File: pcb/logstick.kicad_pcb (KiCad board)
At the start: 2 copper layers, 12 parts, among them IC1 ATTINY85-P, K1 USB, K2 DHT44, K3 SWITCH

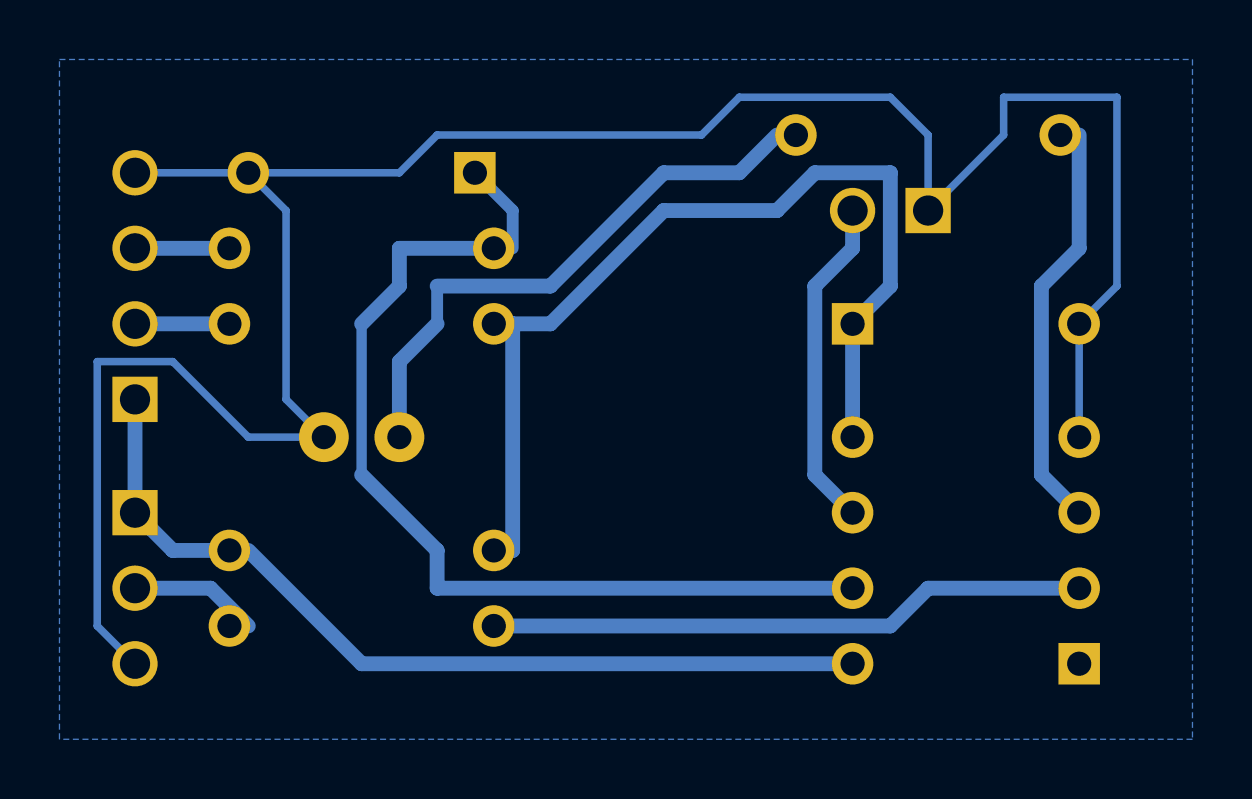
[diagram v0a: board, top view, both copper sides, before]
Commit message: correction R68
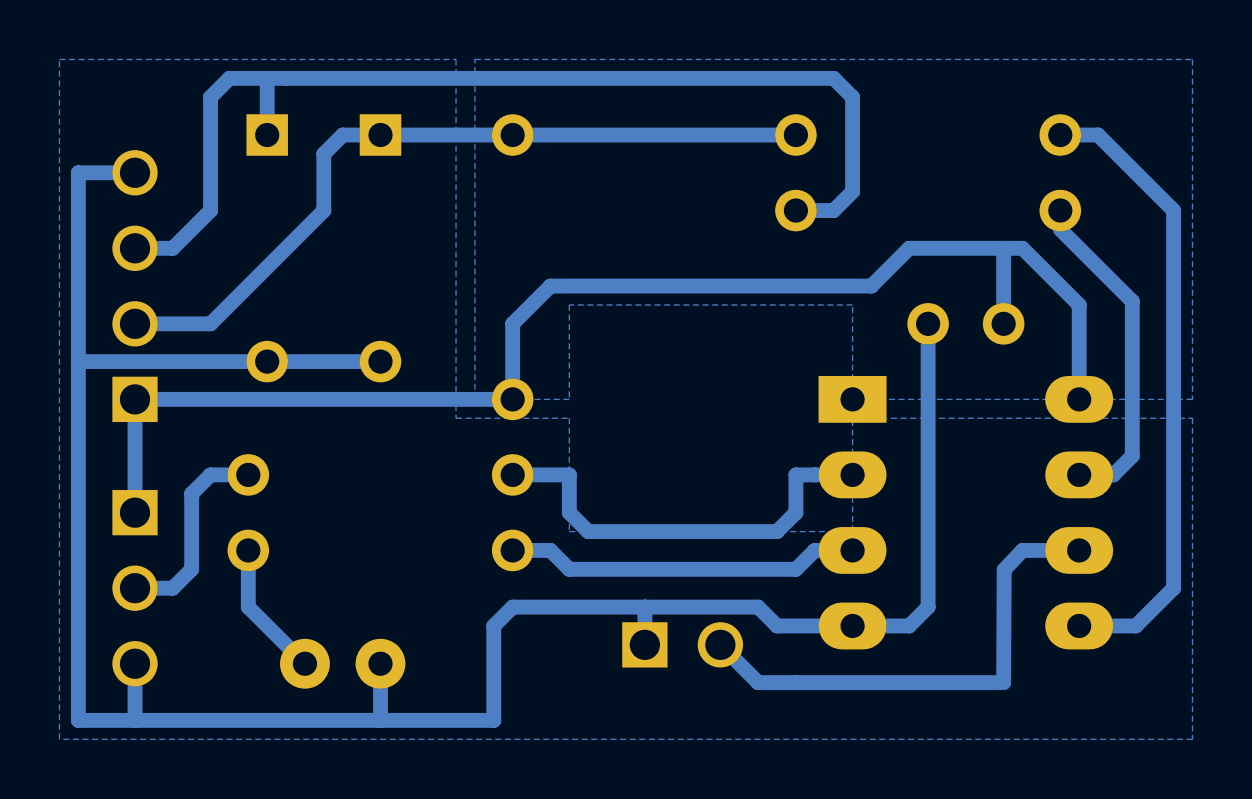
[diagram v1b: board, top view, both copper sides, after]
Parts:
- added C1: 100nF, C1, F.Cu at (71.1, 47.0)
- IC1: footprint DIP-8__300 -> DIP-8__300_ELL
- moved R5 23.1 mm to (51.4, 54.6)
- moved R1 20.1 mm to (69.8, 40.6)
- moved D1 19.8 mm to (51.4, 44.5), turned to 90 degrees
- moved R2 19.1 mm to (69.8, 43.2)
- moved K3 16.2 mm to (61.6, 57.8), turned to 0 degrees
- moved R3 10.8 mm to (55.9, 45.1), turned to 90 degrees
- moved D3 7.65 mm to (50.2, 58.4), turned to 0 degrees
- moved R4 5.12 mm to (51.4, 52.1)
- moved D2 4.07 mm to (47.6, 44.5), turned to 90 degrees
- moved IC1 1.27 mm to (71.1, 53.3), turned to 270 degrees
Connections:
- D2 pad 2: N-0000010 -> N-000008
- IC1 pad 5: N-0000012 -> N-0000011
- K1 pad 2: N-000009 -> N-0000012
- K1 pad 3: N-0000011 -> N-000008
- R1 pad 1: N-000009 -> N-0000012
- R1 pad 2: N-0000012 -> N-0000011
- R2 pad 1: N-0000011 -> N-000008
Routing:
- net N-000008: track 0.00 -> 36.2 mm
- net N-0000010: track 33.9 -> 10.7 mm
- net N-0000011: track 3.17 -> 21.3 mm
- net +5V: track 30.0 -> 45.7 mm
- net N-000003: track 19.8 -> 4.60 mm
- net N-0000012: track 33.7 -> 26.0 mm
- net N-000004: track 20.2 -> 14.5 mm
- net N-000002: track 11.2 -> 16.6 mm
- net N-000009: track 3.17 -> 0.00 mm
- net GND: track 80.7 -> 77.6 mm
- net N-000001: track 14.4 -> 12.0 mm
- net N-000005: track 4.97 -> 6.88 mm
- added copper zone on B.Cu, net +5V
